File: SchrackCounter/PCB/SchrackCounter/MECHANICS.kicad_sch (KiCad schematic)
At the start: 7 parts

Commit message: Schematic update
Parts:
- gave numbers to parts that had none: 7
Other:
- moved on the sheet: C14, C15, R6, SW2, SW3, SW4, SW5

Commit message: Schematic update
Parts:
- added J? (x2): Conn_01x02_Pin, symbol Connector:Conn_01x02_Pin
- added M?: Fan_CPU_4pin, symbol Motor:Fan_CPU_4pin
- added SW? (x3): SW_Push, Button_Switch_SMD:SW_SPST_EVQPE1, symbol Switch:SW_Push
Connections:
- net +3V3: now also J?.2 (Pin_2), SW?.1, SW?.1, SW?.1
- net GND: now also M?.1 (-)
- net TEST PROGRAM 1 renamed DIGIT_SELECT
- net TEST PROGRAM 2 renamed TIME_UP
- new net +5V: M?.2 (+)
- new net MODE: SW?.2
- new net PWM_FAN: M?.4 (PWM)
- new net RESET: SW?.2
- new net RPM: M?.3 (Tacho)
- new net RX: J?.1 (Pin_1)
- new net SCHRACK_SW: J?.1 (Pin_1)
- new net TIME_DOWN: SW?.2
- new net TX: J?.2 (Pin_2)
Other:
- note added: "DEBOUNCE"
- note added: "JST big conductor gauge"
- note added: "Molex 47054-1000"
- moved on the sheet: SW4, SW5

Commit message: sleep, overated imo
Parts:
- J2: renamed from J?; footprint (none) -> Connector_PinHeader_2.54mm:PinHeader_1x02_P2.54mm_Vertical
- J3: renamed from J?; footprint (none) -> Connector_JST:JST_XH_B2B-XH-A_1x02_P2.50mm_Vertical
- M1: renamed from M?; footprint (none) -> Connector:FanPinHeader_1x04_P2.54mm_Vertical
- gave numbers to parts that had none: 3
- renumbered R6 to R10
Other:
- note added: "CONNECTORS"
- note removed: "Molex 47054-1000"
- moved on the sheet: C14, C15, J2, J3, M1, R10, SW2, SW3, SW4, SW5, SW6, SW7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

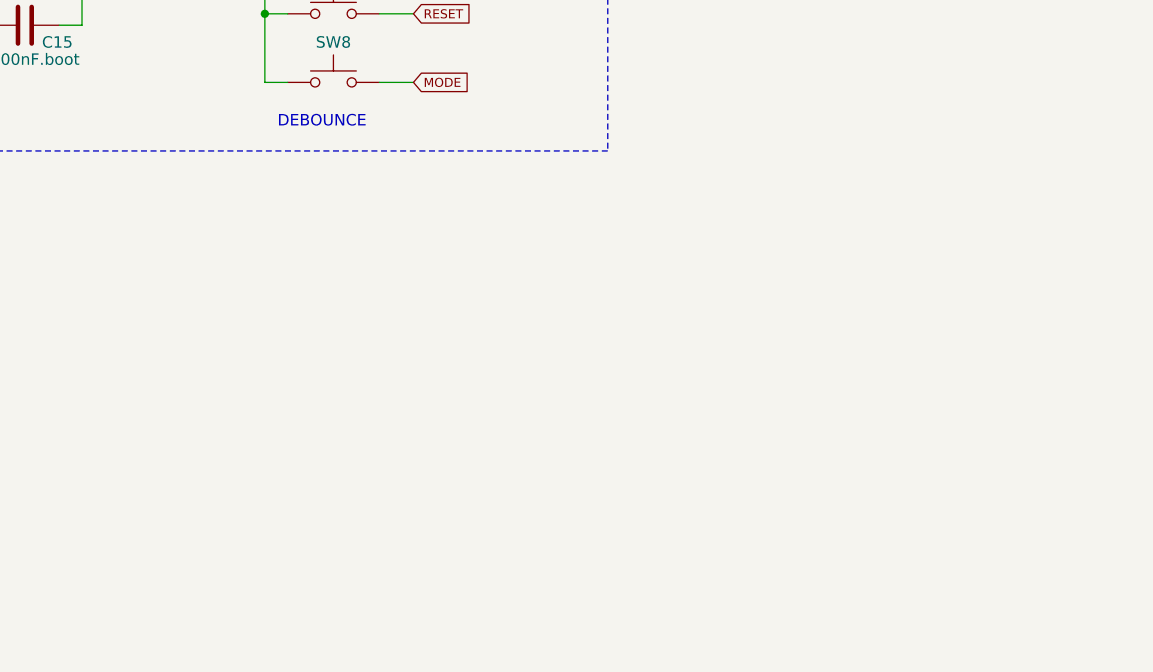
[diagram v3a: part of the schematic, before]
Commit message: libs cleanup, sd card added
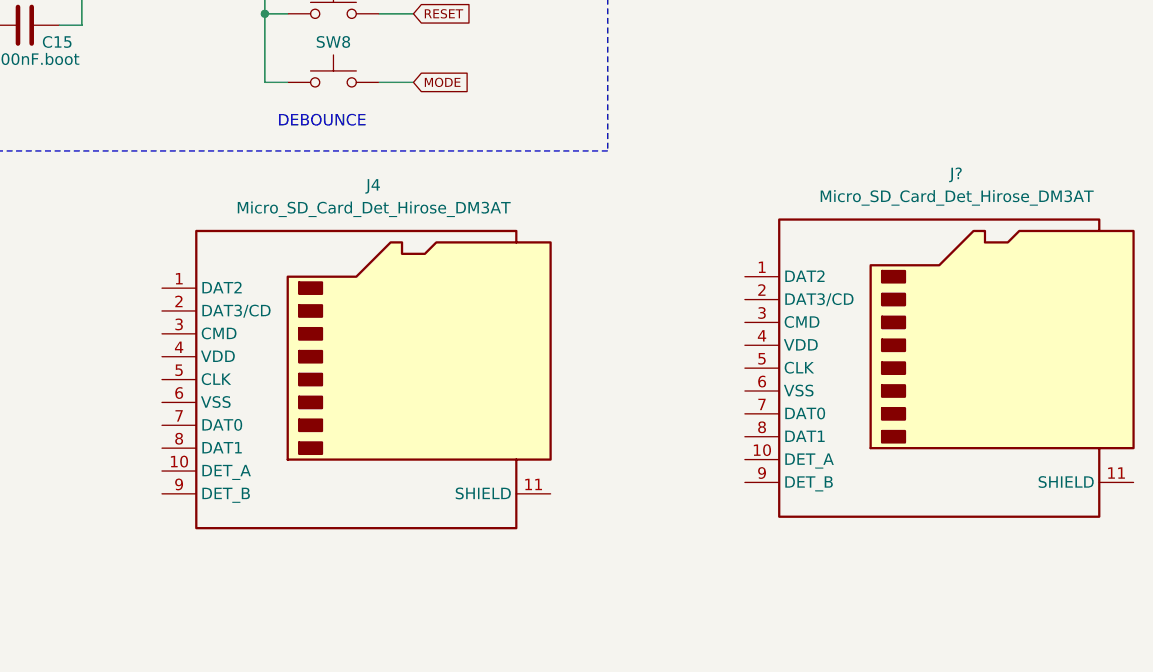
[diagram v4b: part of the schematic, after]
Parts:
- added J4, J?: Micro_SD_Card_Det_Hirose_DM3AT, Connector_Card:microSD_HC_Hirose_DM3AT-SF-PEJM5, symbol Connector:Micro_SD_Card_Det_Hirose_DM3AT
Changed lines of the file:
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@@
+	)
+	(symbol
+		(lib_id "Connector:Micro_SD_Card_Det_Hirose_DM3AT")
+		(at 195.58 118.11 0)
+		(unit 1)
+		(exclude_from_sim no)
+		(in_bom yes)
+		(on_board yes)
+		(dnp no)
+		(fields_autoplaced yes)
+		(property "Reference" "J4"
+			(at 196.215 96.52 0)
+			(effects
+				(font
+					(size 1.27 1.27)
+				)
+			)
+		)
+		(property "Value" "Micro_SD_Card_Det_Hirose_DM3AT"
+			(at 196.215 99.06 0)
+			(effects
+				(font
+					(size 1.27 1.27)
+				)
+			)
+		)
+		(property "Footprint" "Connector_Card:microSD_HC_Hirose_DM3AT-SF-PEJM5"
+			(at 247.65 100.33 0)
+			(effects
+				(font
+					(size 1.27 1.27)
+				)
+				(hide yes)
+			)
+		)
+		(property "Datasheet" "https://www.hirose.com/product/en/download_file/key_name/DM3/category/Catalog/doc_file_id/49662/?file_category_id=4&item_id=195&is_series=1"
+			(at 195.58 115.57 0)
+			(effects
+				(font
+					(size 1.27 1.27)
+				)
+				(hide yes)
+			)
+		)
+		(property "Description" "Micro SD Card Socket with card detection pins"
+			(at 195.58 118.11 0)
+			(effects
+				(font
+					(size 1.27 1.27)
+				)
+				(hide yes)
+			)
+		)
+		(pin "6"
+		)
+		(pin "8"
+		)
+		(pin "1"
+		)
+		(pin "10"
+		)
+		(pin "11"
+		)
+		(pin "7"
+		)
+		(pin "3"
+		)
+		(pin "2"
+		)
+		(pin "9"
+		)
+		(pin "4"
+		)
+		(pin "5"
+		)
+		(instances
+			(project ""
+				(path "/d96f2ffc-3f4c-4f71-b693-29f6b8c3245d/0ccd8f36-c6f2-454f-91e2-c1976b699e0e"
+					(reference "J4")
+					(unit 1)
+				)
+			)
+		)
 	)
 	(symbol
@@
 					(unit 1)
 				)
+			)
+		)
+	)
+	(symbol
+		(lib_id "Connector:Micro_SD_Card_Det_Hirose_DM3AT")
+		(at 260.35 116.84 0)
+		(unit 1)
+		(exclude_from_sim no)
+		(in_bom yes)
+		(on_board yes)
+		(dnp no)
+		(fields_autoplaced yes)
+		(property "Reference" "J?"
+			(at 260.985 95.25 0)
+			(effects
+				(font
+					(size 1.27 1.27)
+				)
+			)
+		)
+		(property "Value" "Micro_SD_Card_Det_Hirose_DM3AT"
+			(at 260.985 97.79 0)
+			(effects
+				(font
+					(size 1.27 1.27)
+				)
+			)
+		)
+		(property "Footprint" "Connector_Card:microSD_HC_Hirose_DM3AT-SF-PEJM5"
+			(at 312.42 99.06 0)
+			(effects
+				(font
+					(size 1.27 1.27)
+				)
+				(hide yes)
+			)
+		)
+		(property "Datasheet" "https://www.hirose.com/product/en/download_file/key_name/DM3/category/Catalog/doc_file_id/49662/?file_category_id=4&item_id=195&is_series=1"
+			(at 260.35 114.3 0)
+			(effects
+				(font
+					(size 1.27 1.27)
+				)
+				(hide yes)
+			)
+		)
+		(property "Description" "Micro SD Card Socket with card detection pins"
+			(at 260.35 116.84 0)
+			(effects
+				(font
+					(size 1.27 1.27)
+				)
+				(hide yes)
+			)
+		)
+		(pin "6"
+		)
+		(pin "8"
+		)
+		(pin "1"
+		)
+		(pin "10"
+		)
+		(pin "11"
+		)
+		(pin "7"
+		)
+		(pin "3"
+		)
+		(pin "2"
+		)
+		(pin "9"
+		)
+		(pin "4"
+		)
+		(pin "5"
+		)
+		(instances
+			(project "SchrackCounter"
+				(path "/d96f2ffc-3f4c-4f71-b693-29f6b8c3245d/0ccd8f36-c6f2-454f-91e2-c1976b699e0e"
+					(reference "J?")
+					(unit 1)
+				)

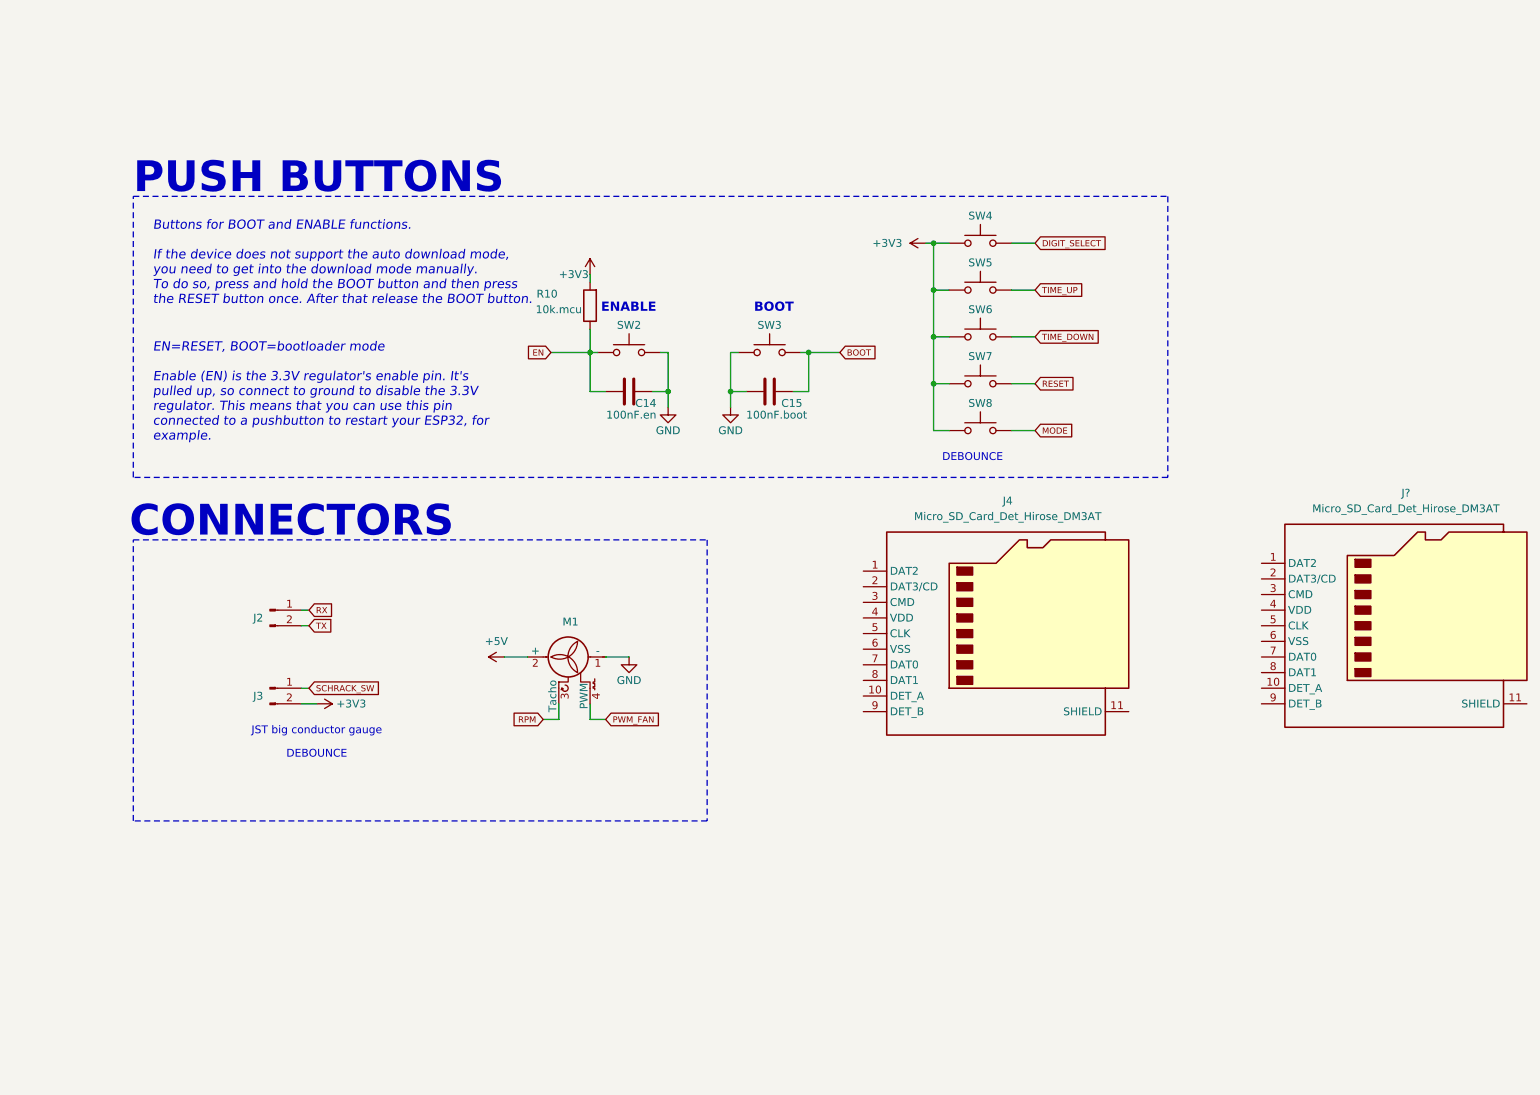
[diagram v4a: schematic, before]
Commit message: SD card addition
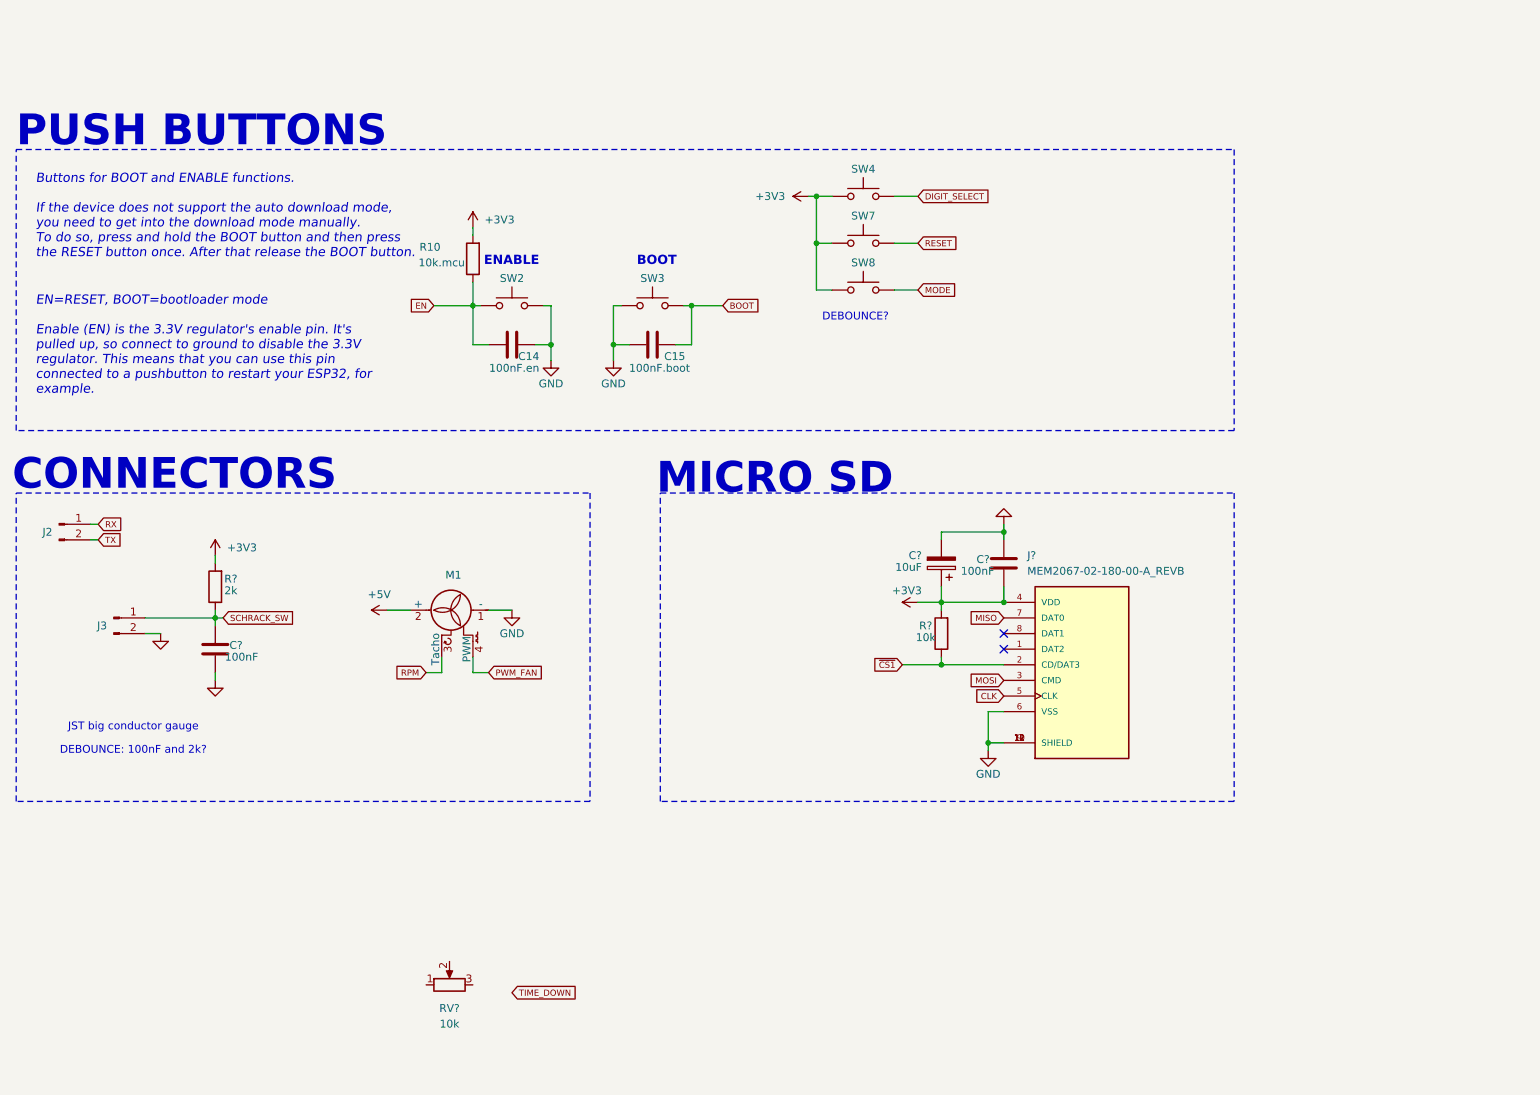
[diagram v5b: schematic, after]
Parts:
- removed J4, J?: Micro_SD_Card_Det_Hirose_DM3AT, Connector_Card:microSD_HC_Hirose_DM3AT-SF-PEJM5, symbol Connector:Micro_SD_Card_Det_Hirose_DM3AT
- removed SW5, SW6: SW_Push, Button_Switch_SMD:SW_SPST_EVQPE1, symbol Switch:SW_Push
- added C?: 10uF, Capacitor_Tantalum_SMD:CP_EIA-3216-18_Kemet-A_Pad1.58x1.35mm_HandSolder, symbol Device:C_Polarized
- added C? (x2): 100nF, Capacitor_SMD:C_0805_2012Metric_Pad1.18x1.45mm_HandSolder, symbol Device:C
- added J?: MEM2067-02-180-00-A_REVB, Schrack_brd:GCT_MEM2067-02-180-00-A_REVB, symbol SchrackThingy_library:MEM2067-02-180-00-A_REVB
- added R?: 2k, Resistor_SMD:R_0805_2012Metric_Pad1.20x1.40mm_HandSolder, symbol Device:R
- added R?: 10k, Resistor_SMD:R_0805_2012Metric_Pad1.20x1.40mm_HandSolder, symbol Device:R
- added RV?: 10k, symbol Device:R_Potentiometer
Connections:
- net +3V3: now also C?.1, C?.1, J?.4 (VDD), R?.2, R?.2; no longer J3.2 (Pin_2)
- net GND: now also J3.2 (Pin_2), C?.1, C?.2, C?.2, J?.10 (SHIELD), J?.11 (SHIELD), J?.12 (SHIELD), J?.6 (VSS), J?.9 (SHIELD)
- net SCHRACK_SW: now also C?.2, R?.1
- new net CLK: J?.5 (CLK)
- new net MISO: J?.7 (DAT0)
- new net MOSI: J?.3 (CMD)
- new net ~{CS1}: J?.2 (CD/DAT3), R?.1
- no-connect marks 0 -> 2
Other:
- note added: "DEBOUNCE: 100nF and 2k?"
- note added: "DEBOUNCE?"
- note added: "MICRO SD"
- note removed: "DEBOUNCE"
- moved on the sheet: C14, C15, J2, J3, M1, R10, SW2, SW3, SW4, SW7, SW8

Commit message: Footprint reorder, schematic and pcb update
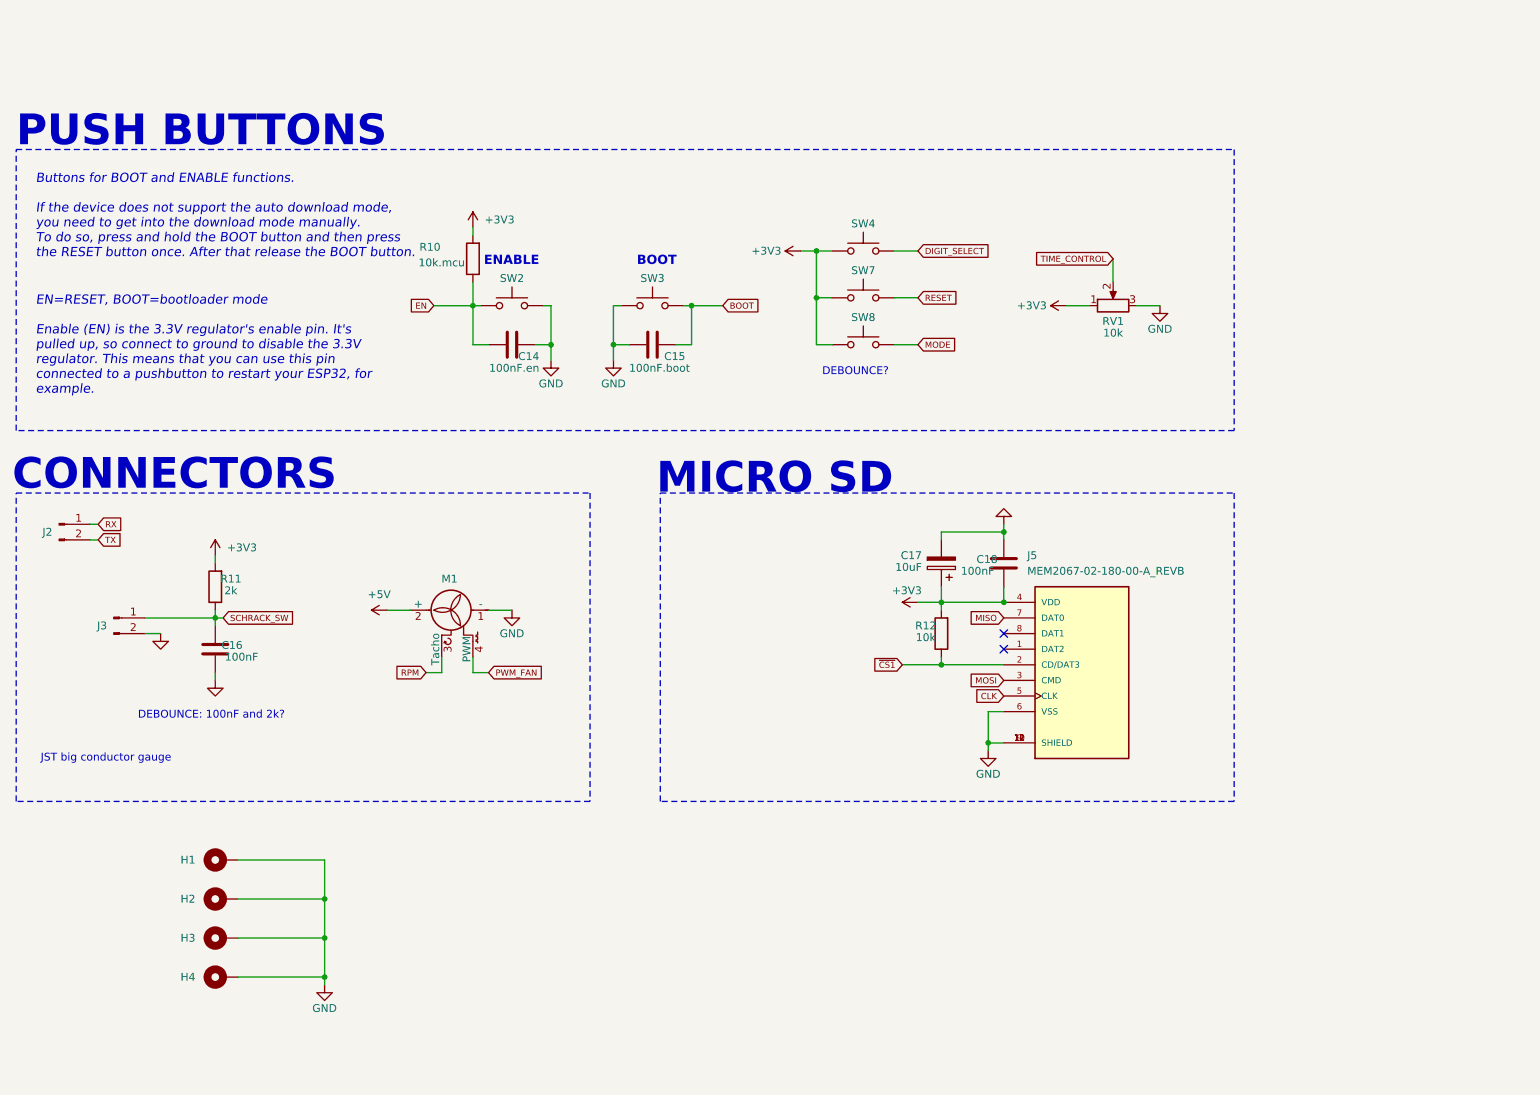
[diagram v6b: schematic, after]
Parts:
- added H1, H2, H3, H4: Mounting Hole M3, MountingHole:MountingHole_3.2mm_M3_Pad_Via, symbol Mechanical:MountingHole_Pad
- SW4, SW7: footprint Button_Switch_SMD:SW_SPST_EVQPE1 -> Connector_JST:JST_XH_B2B-XH-A_1x02_P2.50mm_Vertical
- gave numbers to parts that had none: 7
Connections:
- net +3V3: now also RV1.1
- net GND: now also RV1.3, H1.1, H2.1, H3.1, H4.1
- net TIME_CONTROL: now reaches RV1.2
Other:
- moved on the sheet: RV1, SW4, SW7, SW8

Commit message: PCB update
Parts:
- added C19, C20: 100nF, Capacitor_SMD:C_0805_2012Metric_Pad1.18x1.45mm_HandSolder, symbol Device:C
- added SW6: RotaryEncoder_Switch, Connector_JST:JST_XH_B4B-XH-A_1x04_P2.50mm_Vertical, symbol SchrackThingy_library:RotaryEncoder_Switch
- J5: footprint Schrack_brd:GCT_MEM2067-02-180-00-A_REVB -> Schrack_brd:MICRO_SD_CARD
- RV1: footprint (none) -> Connector_JST:JST_XH_B3B-XH-A_1x03_P2.50mm_Vertical
- renumbered C16 to C14, C14 to C15, C15 to C16, J2 to J3, J3 to J4, R11 to R10, R10 to R11, SW2 to SW1, SW3 to SW2, SW4 to SW3, SW7 to SW4, SW8 to SW5
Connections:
- net GND: now also SW6.2 (C), SW6.5 (S2)
- new net: C19.2, SW6.1 (A)
- new net: C20.1, SW6.3 (B)
- new net ENCODER_SWITCH: SW6.4 (S1)
- new net TIME_CONTROL_CLK: C20.2
- new net TIME_CONTROL_CT: C19.1
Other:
- moved on the sheet: C14, C15, C16, C17, C18, H1, H2, H3, H4, J3, J4, J5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

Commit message: schematic and board update
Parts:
- removed C19: 100nF, Capacitor_SMD:C_0805_2012Metric_Pad1.18x1.45mm_HandSolder, symbol Device:C
- removed RV1: 10k, Connector_JST:JST_XH_B3B-XH-A_1x03_P2.50mm_Vertical, symbol Device:R_Potentiometer
- removed SW3: SW_Push, Connector_JST:JST_XH_B2B-XH-A_1x02_P2.50mm_Vertical, symbol Switch:SW_Push
- removed SW5: SW_Push, Button_Switch_SMD:SW_SPST_EVQPE1, symbol Switch:SW_Push
- removed SW6: RotaryEncoder_Switch, Connector_JST:JST_XH_B4B-XH-A_1x04_P2.50mm_Vertical, symbol SchrackThingy_library:RotaryEncoder_Switch
- added C17: 100nF, Capacitor_SMD:C_0805_2012Metric_Pad1.18x1.45mm_HandSolder, symbol Device:C
- added R12, R14: 2k, Resistor_SMD:R_0805_2012Metric_Pad1.20x1.40mm_HandSolder, symbol Device:R
- added SW4: SW_Push, Connector_JST:JST_XH_B2B-XH-A_1x02_P2.50mm_Vertical, symbol Switch:SW_Push
- C20: LCSC C49678 -> (none)
- renumbered C17 to C18, C18 to C19, R12 to R13, SW4 to SW3
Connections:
- net TIME_CONTROL_CLK is gone; now on net MODE: C20.2
- net +3V3: now also R12.2, R14.2; no longer SW3.1
- net GND: now also C20.1, SW3.1, C17.1, SW4.1
- net MODE: now also R14.1, SW4.2
- net RESET: now also C17.2, R12.1
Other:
- note added: "MOUNTING HOLES"
- note added: "PREDIFINED TIME, CHANGING USING WEBSERVER"
- note removed: "DEBOUNCE?"
- moved on the sheet: C15, C16, H1, H2, H3, H4, R11, SW1, SW2, SW3
